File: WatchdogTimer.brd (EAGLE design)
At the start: 22.4 x 15 mm, 20 parts, among them IC1 LM555D, Q2 MOSFET-NCHANNELSMD

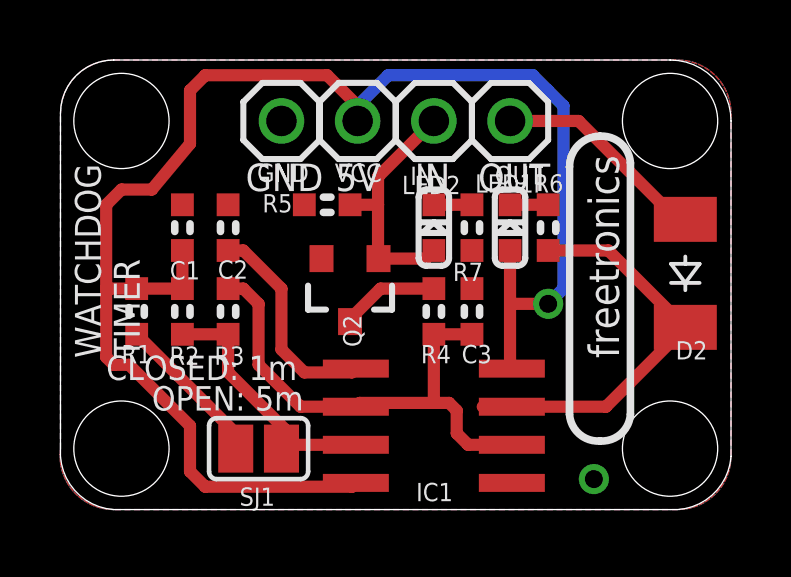
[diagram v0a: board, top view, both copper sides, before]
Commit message: Replaced main timing cap with 1206 tantalum for size reasons Updates to routing and labels
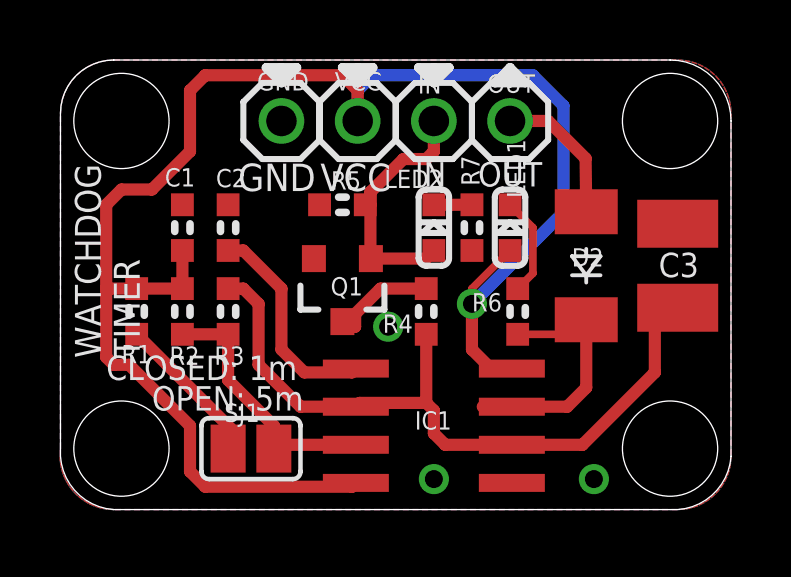
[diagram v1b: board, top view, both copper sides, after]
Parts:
- removed Q2: MOSFET-NCHANNELSMD, freetronics-original:SOT23-3
- added Q1: 2N7002, freetronics-original:SOT23-3
- C3: value 100uF -> 100uF 10V 1210 ceramic; device freetronics-master-v1:0603 -> freetronics-jon:C1210
- moved C3 7.03 mm to (20.6, 8.13)
- moved D2 3.31 mm to (17.5, 8.13)
- moved R6 2.97 mm to (15.2, 6.60)
- moved R5 0.51 mm to (9.40, 10.2)
- moved SJ1 0.25 mm to (6.35, 2.03)
- moved R4 0.25 mm to (12.2, 6.60)
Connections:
- net GND: now also Q1.2; no longer Q2.2
- net N$1: now also Q1.3; no longer Q2.3
- net RST: now also Q1.1; no longer Q2.1
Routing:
- net C4: track 16.9 -> 24.0 mm
- net TO: track 13.5 -> 8.41 mm
- net N$8: track 7.20 -> 4.81 mm
- net N$5: track 1.27 -> 3.32 mm
- net VCC: track 52.6 -> 54.5 mm
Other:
- board text added: "(c) 2014 Freetronics"
- board text added: "A"
- board text added: "K"
- board text added: "VCC"
- board text added: "tron.cc/dog"
- board text removed: "(c) 2013 Freetronics"
- board text removed: "5V"
- board text removed: "www.freetronics.com/dog"
